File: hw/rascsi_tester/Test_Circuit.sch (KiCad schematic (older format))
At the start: 4 parts

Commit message: Updated tester board
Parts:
- D1: footprint LED_SMD:LED_1206_3216Metric -> LED_SMD:LED_0805_2012Metric; LCSC (none) -> C2297
- R1: footprint Resistor_SMD:R_1206_3216Metric_Pad1.42x1.75mm_HandSolder -> Resistor_SMD:R_0805_2012Metric; LCSC (none) -> C17557
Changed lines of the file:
@@
 $Descr A4 11693 8268
 encoding utf-8
-Sheet 5 20
+Sheet 18 20
 Title ""
 Date ""
@@
 AR Path="/5F47F75E/5F449624" Ref="D18"  Part="1"
 AR Path="/5F47F761/5F449624" Ref="D19"  Part="1"
-F 0 "D4" V 4346 3232 50  0000 R CNN
+F 0 "D17" V 4346 3232 50  0000 R CNN
 F 1 "LED_Small" V 4255 3232 50  0000 R CNN
-F 2 "LED_SMD:LED_1206_3216Metric" V 4300 3300 50  0001 C CNN
+F 2 "LED_SMD:LED_0805_2012Metric" V 4300 3300 50  0001 C CNN
 F 3 "~" V 4300 3300 50  0001 C CNN
+F 4 "C2297" V 4300 3300 50  0001 C CNN "LCSC"
 	1    4300 3300
 	0    -1   -1   0
@@
 AR Path="/5F47F75E/5F44A7C9" Ref="JP35"  Part="1"
 AR Path="/5F47F761/5F44A7C9" Ref="JP37"  Part="1"
-F 0 "JP7" H 4300 3205 50  0000 C CNN
+F 0 "JP33" H 4300 3205 50  0000 C CNN
 F 1 "SolderJumper_3_Bridged12" H 4300 3114 50  0000 C CNN
 F 2 "Jumper:SolderJumper-3_P1.3mm_Bridged12_Pad1.0x1.5mm" H 4300 3000 50  0001 C CNN
@@
 AR Path="/5F47F75E/5F44F202" Ref="JP36"  Part="1"
 AR Path="/5F47F761/5F44F202" Ref="JP38"  Part="1"
-F 0 "JP8" H 4300 4113 50  0000 C CNN
+F 0 "JP34" H 4300 4113 50  0000 C CNN
 F 1 "SolderJumper_3_Bridged12" H 4300 4204 50  0000 C CNN
 F 2 "Jumper:SolderJumper-3_P1.3mm_Bridged12_Pad1.0x1.5mm" H 4300 4000 50  0001 C CNN
@@
 AR Path="/5F47F75E/5F44FD73" Ref="#PWR055"  Part="1"
 AR Path="/5F47F761/5F44FD73" Ref="#PWR057"  Part="1"
-F 0 "#PWR027" H 4500 2850 50  0001 C CNN
+F 0 "#PWR053" H 4500 2850 50  0001 C CNN
 F 1 "+5V" V 4515 3128 50  0000 L CNN
 F 2 "" H 4500 3000 50  0001 C CNN
@@
 AR Path="/5F47F75E/5F4502AD" Ref="#PWR056"  Part="1"
 AR Path="/5F47F761/5F4502AD" Ref="#PWR058"  Part="1"
-F 0 "#PWR028" H 4500 3750 50  0001 C CNN
+F 0 "#PWR054" H 4500 3750 50  0001 C CNN
 F 1 "GND" V 4505 3872 50  0000 R CNN
 F 2 "" H 4500 4000 50  0001 C CNN
@@
 AR Path="/5F47F75E/5F454172" Ref="R18"  Part="1"
 AR Path="/5F47F761/5F454172" Ref="R19"  Part="1"
-F 0 "R4" H 4359 3696 50  0000 L CNN
+F 0 "R17" H 4359 3696 50  0000 L CNN
 F 1 "220" H 4359 3605 50  0000 L CNN
-F 2 "Resistor_SMD:R_1206_3216Metric_Pad1.42x1.75mm_HandSolder" H 4300 3650 50  0001 C CNN
+F 2 "Resistor_SMD:R_0805_2012Metric" H 4300 3650 50  0001 C CNN
 F 3 "~" H 4300 3650 50  0001 C CNN
+F 4 "C17557" H 4300 3650 50  0001 C CNN "LCSC"
 	1    4300 3650
 	1    0    0    -1

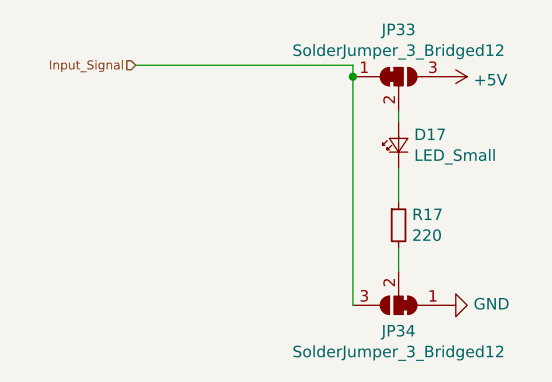
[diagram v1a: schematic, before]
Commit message: Cleanup LCSC part number, regenerate gerbers and re-generate schematics
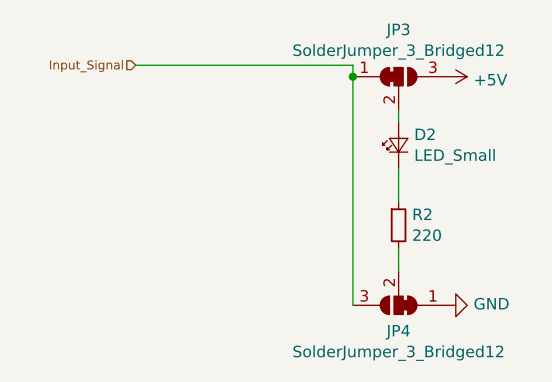
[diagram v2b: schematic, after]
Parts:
- D1: LCSC C2297 -> C125090
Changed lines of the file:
@@
 EESchema Schematic File Version 4
+LIBS:rascsi_tester-cache
 EELAYER 30 0
 EELAYER END
 $Descr A4 11693 8268
 encoding utf-8
-Sheet 18 20
+Sheet 3 20
 Title ""
 Date ""
@@
 AR Path="/5F47F75E/5F449624" Ref="D18"  Part="1"
 AR Path="/5F47F761/5F449624" Ref="D19"  Part="1"
-F 0 "D17" V 4346 3232 50  0000 R CNN
+F 0 "D2" V 4346 3232 50  0000 R CNN
 F 1 "LED_Small" V 4255 3232 50  0000 R CNN
 F 2 "LED_SMD:LED_0805_2012Metric" V 4300 3300 50  0001 C CNN
 F 3 "~" V 4300 3300 50  0001 C CNN
-F 4 "C2297" V 4300 3300 50  0001 C CNN "LCSC"
+F 4 " C125090" V 4300 3300 50  0001 C CNN "LCSC"
 	1    4300 3300
 	0    -1   -1   0
@@
 AR Path="/5F47F75E/5F44A7C9" Ref="JP35"  Part="1"
 AR Path="/5F47F761/5F44A7C9" Ref="JP37"  Part="1"
-F 0 "JP33" H 4300 3205 50  0000 C CNN
+F 0 "JP3" H 4300 3205 50  0000 C CNN
 F 1 "SolderJumper_3_Bridged12" H 4300 3114 50  0000 C CNN
 F 2 "Jumper:SolderJumper-3_P1.3mm_Bridged12_Pad1.0x1.5mm" H 4300 3000 50  0001 C CNN
@@
 AR Path="/5F47F75E/5F44F202" Ref="JP36"  Part="1"
 AR Path="/5F47F761/5F44F202" Ref="JP38"  Part="1"
-F 0 "JP34" H 4300 4113 50  0000 C CNN
+F 0 "JP4" H 4300 4113 50  0000 C CNN
 F 1 "SolderJumper_3_Bridged12" H 4300 4204 50  0000 C CNN
 F 2 "Jumper:SolderJumper-3_P1.3mm_Bridged12_Pad1.0x1.5mm" H 4300 4000 50  0001 C CNN
@@
 AR Path="/5F47F75E/5F44FD73" Ref="#PWR055"  Part="1"
 AR Path="/5F47F761/5F44FD73" Ref="#PWR057"  Part="1"
-F 0 "#PWR053" H 4500 2850 50  0001 C CNN
+F 0 "#PWR023" H 4500 2850 50  0001 C CNN
 F 1 "+5V" V 4515 3128 50  0000 L CNN
 F 2 "" H 4500 3000 50  0001 C CNN
@@
 AR Path="/5F47F75E/5F4502AD" Ref="#PWR056"  Part="1"
 AR Path="/5F47F761/5F4502AD" Ref="#PWR058"  Part="1"
-F 0 "#PWR054" H 4500 3750 50  0001 C CNN
+F 0 "#PWR024" H 4500 3750 50  0001 C CNN
 F 1 "GND" V 4505 3872 50  0000 R CNN
 F 2 "" H 4500 4000 50  0001 C CNN
@@
 AR Path="/5F47F75E/5F454172" Ref="R18"  Part="1"
 AR Path="/5F47F761/5F454172" Ref="R19"  Part="1"
-F 0 "R17" H 4359 3696 50  0000 L CNN
+F 0 "R2" H 4359 3696 50  0000 L CNN
 F 1 "220" H 4359 3605 50  0000 L CNN
 F 2 "Resistor_SMD:R_0805_2012Metric" H 4300 3650 50  0001 C CNN
